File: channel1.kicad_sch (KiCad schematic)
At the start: 58 parts, among them IC1 TLV73325PDBVT, IC2 TLV73312PDBVT, J2 47151-1001, J3 5051101992, U1 TC358742XBG, U2 TPD8S009DSMR, U3 PCA9517ATP, Y1 7C-27.000MBB-T

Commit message: [#58304] Perform globlib
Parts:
- C1, C12, C14, C15, C2, C22, C27, C28, C29, C3, C30: footprint antmicro-hdmi-mipi-bridge-hw-footprints:C_0402_1005Metric -> antmicro-footprints:C_0402_1005Metric; symbol antmicro-hdmi-mipi-bridge-hw:C_100n_0402 -> antmicroCapacitors0402:C_100n_0402
- C10, C11, C8, C9: footprint antmicro-hdmi-mipi-bridge-hw-footprints:C_0603_1608Metric -> antmicro-footprints:C_0603_1608Metric; symbol antmicro-hdmi-mipi-bridge-hw:C_4u7_0603 -> antmicroCapacitors0603:C_4u7_0603
- C13, C16, C21, C23: footprint antmicro-hdmi-mipi-bridge-hw-footprints:C_0402_1005Metric -> antmicro-footprints:C_0402_1005Metric; symbol antmicro-hdmi-mipi-bridge-hw:C_47p_0402 -> antmicroCapacitors0402:C_47p_0402
- C17, C18, C19, C20: footprint antmicro-hdmi-mipi-bridge-hw-footprints:C_0603_1608Metric -> antmicro-footprints:C_0603_1608Metric; symbol antmicro-hdmi-mipi-bridge-hw:C_10u_0603 -> antmicroCapacitors0603:C_10u_0603
- C4, C5, C6, C7: footprint antmicro-hdmi-mipi-bridge-hw-footprints:C_0402_1005Metric -> antmicro-footprints:C_0402_1005Metric; symbol antmicro-hdmi-mipi-bridge-hw:C_470p_0402 -> antmicroCapacitors0402:C_470p_0402
- FB1: footprint antmicro-hdmi-mipi-bridge-hw-footprints:FB_0603_1608Metric -> antmicro-footprints:FB_0603_1608Metric; symbol antmicro-hdmi-mipi-bridge-hw:FB_120Z_3A_0603 -> antmicroFerriteBeadsandChips:FB_120Z_3A_Murata-BLM18SG_0603
- FB2, FB3, FB4, FB5: footprint antmicro-hdmi-mipi-bridge-hw-footprints:FB_0805_2012Metric -> antmicro-footprints:FB_0805_2012Metric; symbol antmicro-hdmi-mipi-bridge-hw:FB_1000Z_0.8A_0805 -> antmicroFerriteBeadsandChips:FB_1kZ_0.8A_WE-CBF_0805
- FB6: footprint antmicro-hdmi-mipi-bridge-hw-footprints:FB_0603_1608Metric -> antmicro-footprints:FB_0603_1608Metric; symbol antmicro-hdmi-mipi-bridge-hw:FB_600Z_0.5A_0603 -> antmicroFerriteBeadsandChips:FB_600Z_0.5A_Murata-BLM18AG_0603
- IC1: footprint antmicro-hdmi-mipi-bridge-hw-footprints:SOT-23-5 -> antmicro-footprints:SOT-23-5; symbol antmicro-hdmi-mipi-bridge-hw:TLV73325PDBVT -> antmicroPMICVoltageRegulatorsLinear:TLV73325PDBVT
- IC2: footprint antmicro-hdmi-mipi-bridge-hw-footprints:SOT-23-5 -> antmicro-footprints:SOT-23-5; symbol antmicro-hdmi-mipi-bridge-hw:TLV73312PDBVT -> antmicroPMICVoltageRegulatorsLinear:TLV73312PDBVT
- J3: footprint antmicro-hdmi-mipi-bridge-hw-footprints:5051101992 -> antmicro-footprints:5051101992; symbol antmicro-hdmi-mipi-bridge-hw:5051101992 -> antmicroFCCConnectors:5051101992
- R1, R2, R5, R6, R7, R8: footprint antmicro-hdmi-mipi-bridge-hw-footprints:R_0603_1608Metric -> antmicro-footprints:R_0603_1608Metric; symbol antmicro-hdmi-mipi-bridge-hw:R_0R_0603 -> antmicroResistors0603:R_0R_0603
- R10, R11, R12, R3, R9: footprint antmicro-hdmi-mipi-bridge-hw-footprints:R_0402_1005Metric -> antmicro-footprints:R_0402_1005Metric; symbol antmicro-hdmi-mipi-bridge-hw:R_10k_0402 -> antmicroResistors0402:R_10k_0402
- R13: footprint antmicro-hdmi-mipi-bridge-hw-footprints:R_0402_1005Metric -> antmicro-footprints:R_0402_1005Metric; symbol antmicro-hdmi-mipi-bridge-hw:R_22R_0402 -> antmicroResistors0402:R_22R_0402
- R4: footprint antmicro-hdmi-mipi-bridge-hw-footprints:R_0402_1005Metric -> antmicro-footprints:R_0402_1005Metric; symbol antmicro-hdmi-mipi-bridge-hw:R_2k_0402 -> antmicroResistors0402:R_2k_0402
- TP1, TP2, TP3, TP4: footprint antmicro-hdmi-mipi-bridge-hw-footprints:TP_SMD_0.75mm -> antmicro-footprints:TP_SMD_0.75mm; symbol antmicro-hdmi-mipi-bridge-hw:TP_0.75mm_SMD -> antmicroTestPoints:TP_0.75mm_SMD
- U1: footprint antmicro-hdmi-mipi-bridge-hw-footprints:BGA-64_8x8_6.0x6.0mm -> antmicro-footprints:BGA-64_8x8_6.0x6.0mm; symbol antmicro-hdmi-mipi-bridge-hw:TC358742XBG -> antmicroInterfaceControllers:TC358742XBG
- U2: footprint antmicro-hdmi-mipi-bridge-hw-footprints:R-PDSO-N15 -> antmicro-footprints:R-PDSO-N15; symbol antmicro-hdmi-mipi-bridge-hw:TPD8S009DSMR -> antmicroTVSDiodes:TPD8S009DSMR
- U3: footprint antmicro-hdmi-mipi-bridge-hw-footprints:SOT1069-2 -> antmicro-footprints:SOT1069-2; symbol antmicro-hdmi-mipi-bridge-hw:PCA9517ATP -> antmicroLogicTranslatorsLevelShifters:PCA9517ATP
- Y1: footprint antmicro-hdmi-mipi-bridge-hw-footprints:7C-24.000MBB-T -> antmicro-footprints:Oscillator_SMD_TXC_7C_5x3.2x1.2mm; symbol antmicro-hdmi-mipi-bridge-hw:7C-27.000MBB-T -> antmicroOscillators:Oscillator_27MHz_TXC_7C

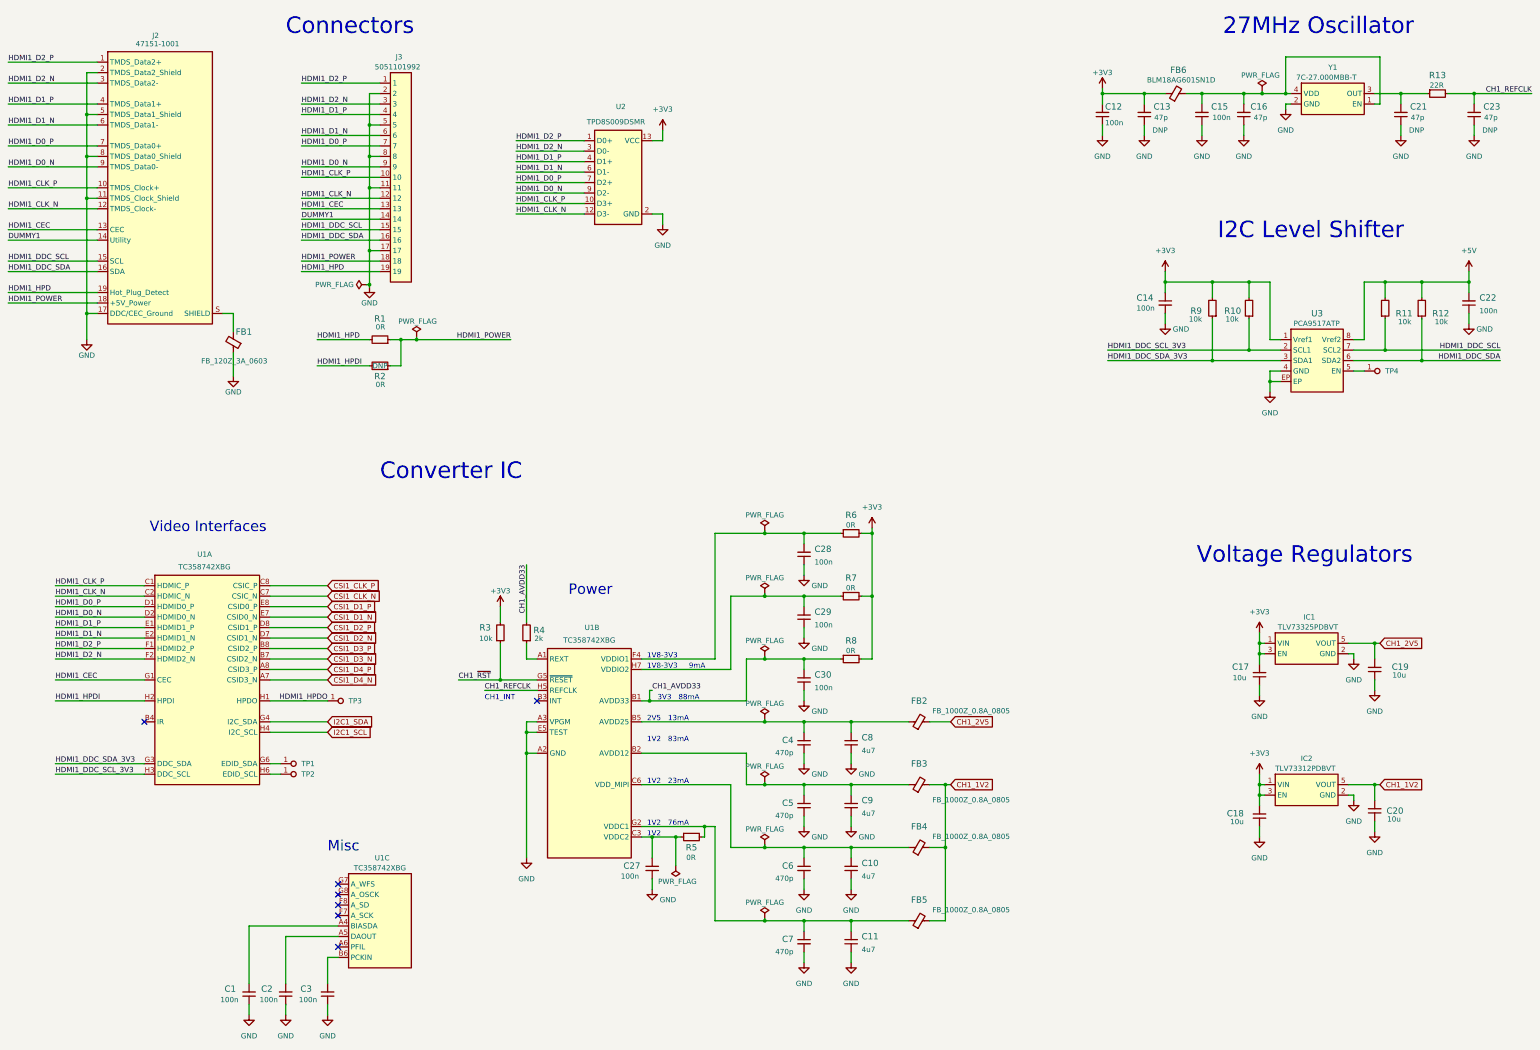
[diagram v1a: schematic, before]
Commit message: [#58304] Update symbols to global libs
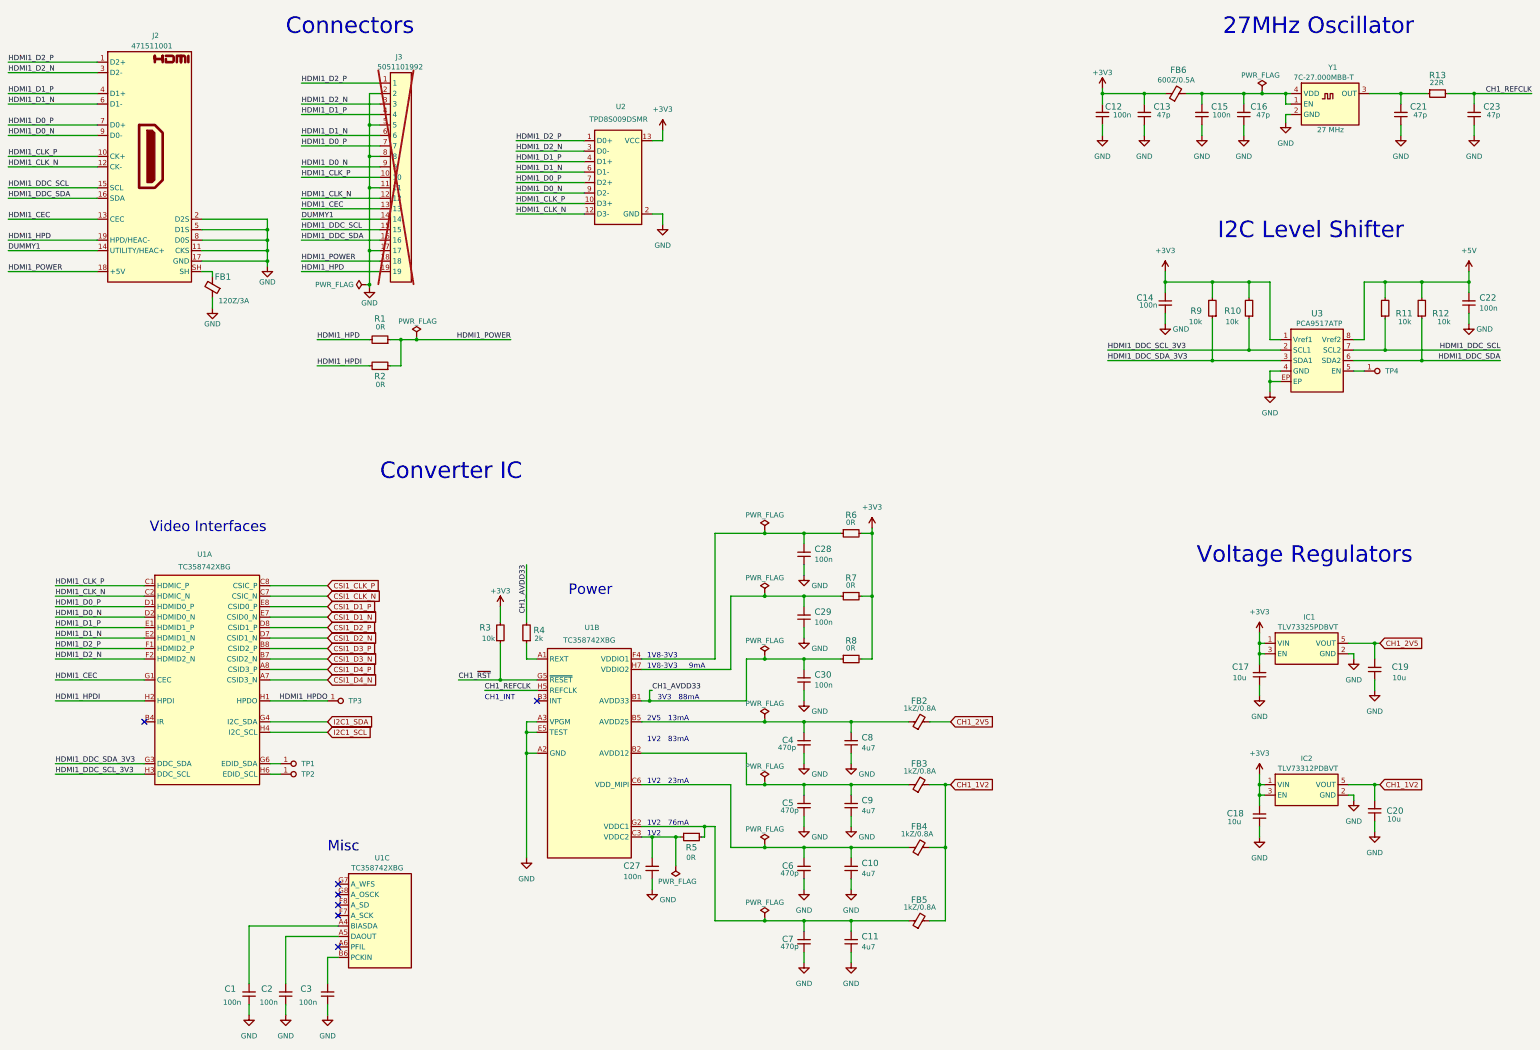
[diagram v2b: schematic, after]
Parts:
- C13, C21, C23: DNP DNP -> (none); MPN GRM1555C1E470JA01D -> C0402C470J5GACTU; Manufacturer Murata -> KEMET
- C16: MPN GRM1555C1E470JA01D -> C0402C470J5GACTU; Manufacturer Murata -> KEMET
- C17, C18, C19, C20: Dielectric (none) -> template_dielectric
- FB1: value FB_120Z_3A_0603 -> FB_120Z_3A_Murata-BLM18SG_0603; Val (none) -> 120Z/3A
- FB2, FB3, FB4, FB5: value FB_1000Z_0.8A_0805 -> FB_1kZ_0.8A_WE-CBF_0805; Val (none) -> 1kZ/0.8A
- FB6: value FB_600Z_0.5A_0603 -> FB_600Z_0.5A_Murata-BLM18AG_0603; Val (none) -> 600Z/0.5A
- J2: value 47151-1001 -> HDMI-A_Molex_471511001; footprint antmicro-hdmi-mipi-bridge-hw-footprints:47151-1001 -> antmicro-footprints:HDMI-A_Receptacle_Molex_471511001; symbol antmicro-hdmi-mipi-bridge-hw:47151-1001 -> antmicroVideoConnectors:HDMI-A_Molex_471511001; MPN 47151-1001 -> 471511001
- J3: now not fitted
- R2: DNP DNP -> (none)
- Y1: value 7C-27.000MBB-T -> Oscillator_27MHz_TXC_7C; Val (none) -> 27 MHz
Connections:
- net at FB1.2: now also J2.SH; no longer J2.S (SHIELD)
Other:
- moved on the sheet: FB1
